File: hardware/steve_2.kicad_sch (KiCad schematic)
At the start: 24 parts, among them J6 MicroSD_Hirose_DM3AT, U2 TI_TPS51386RJNR_Regulator_Buc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, U6 W25Q128JVSIQ

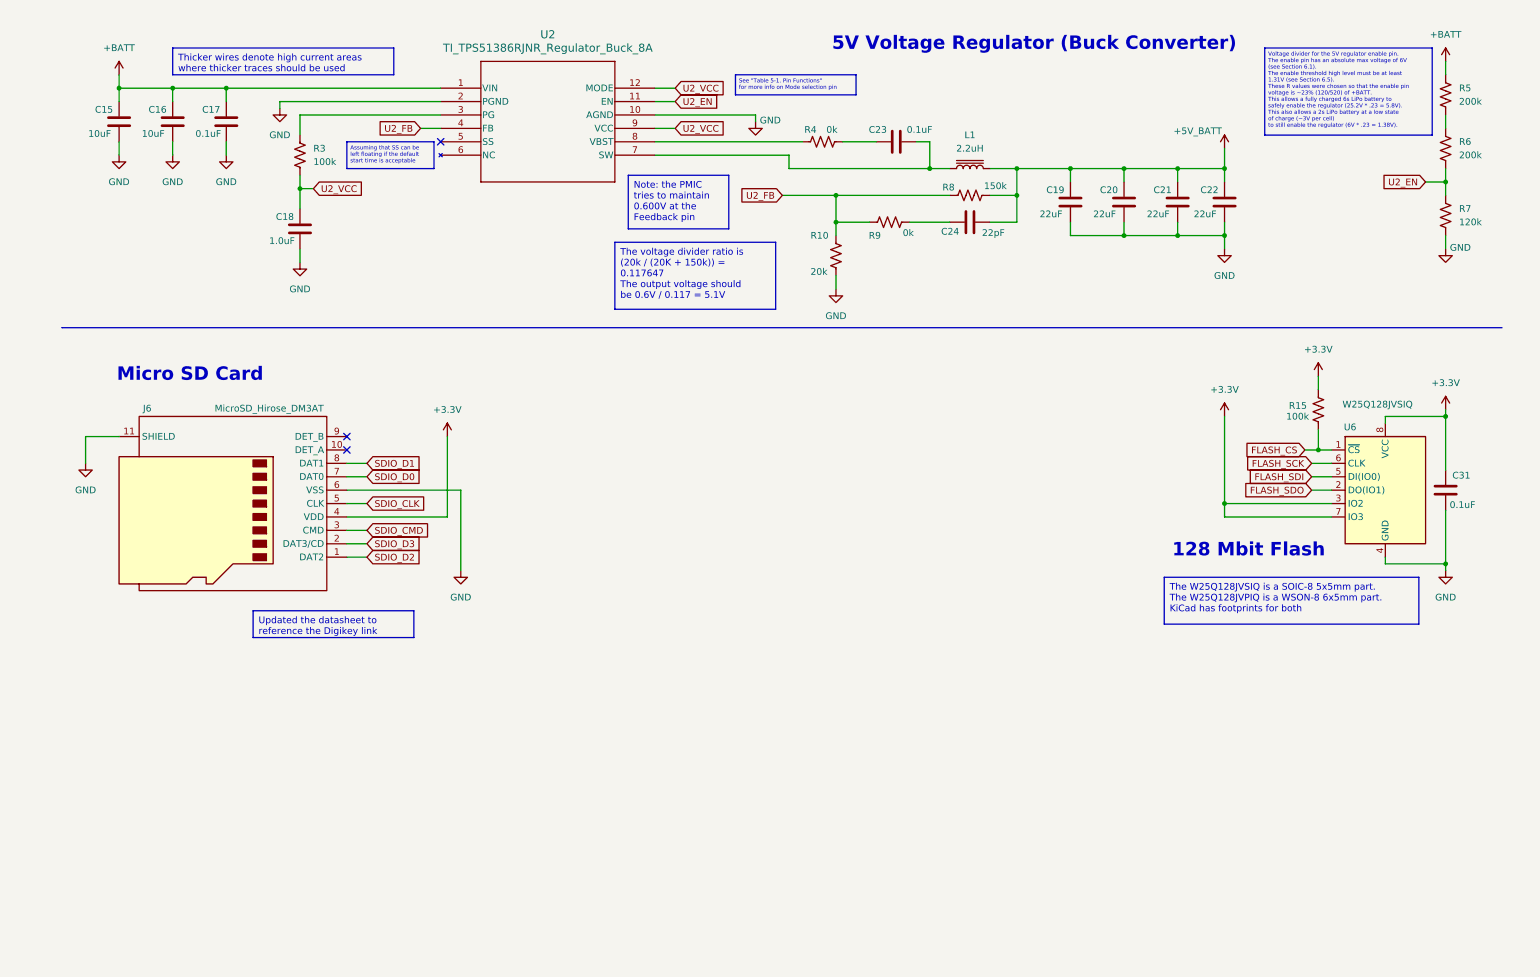
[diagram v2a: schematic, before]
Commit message: Add components to schematic; fix existing ones
Added additional components to schematic such as IO connectors. Replaced the 10A TO-263-2 diode rectifiers with much smaller 5A ones.
Other various fixes.
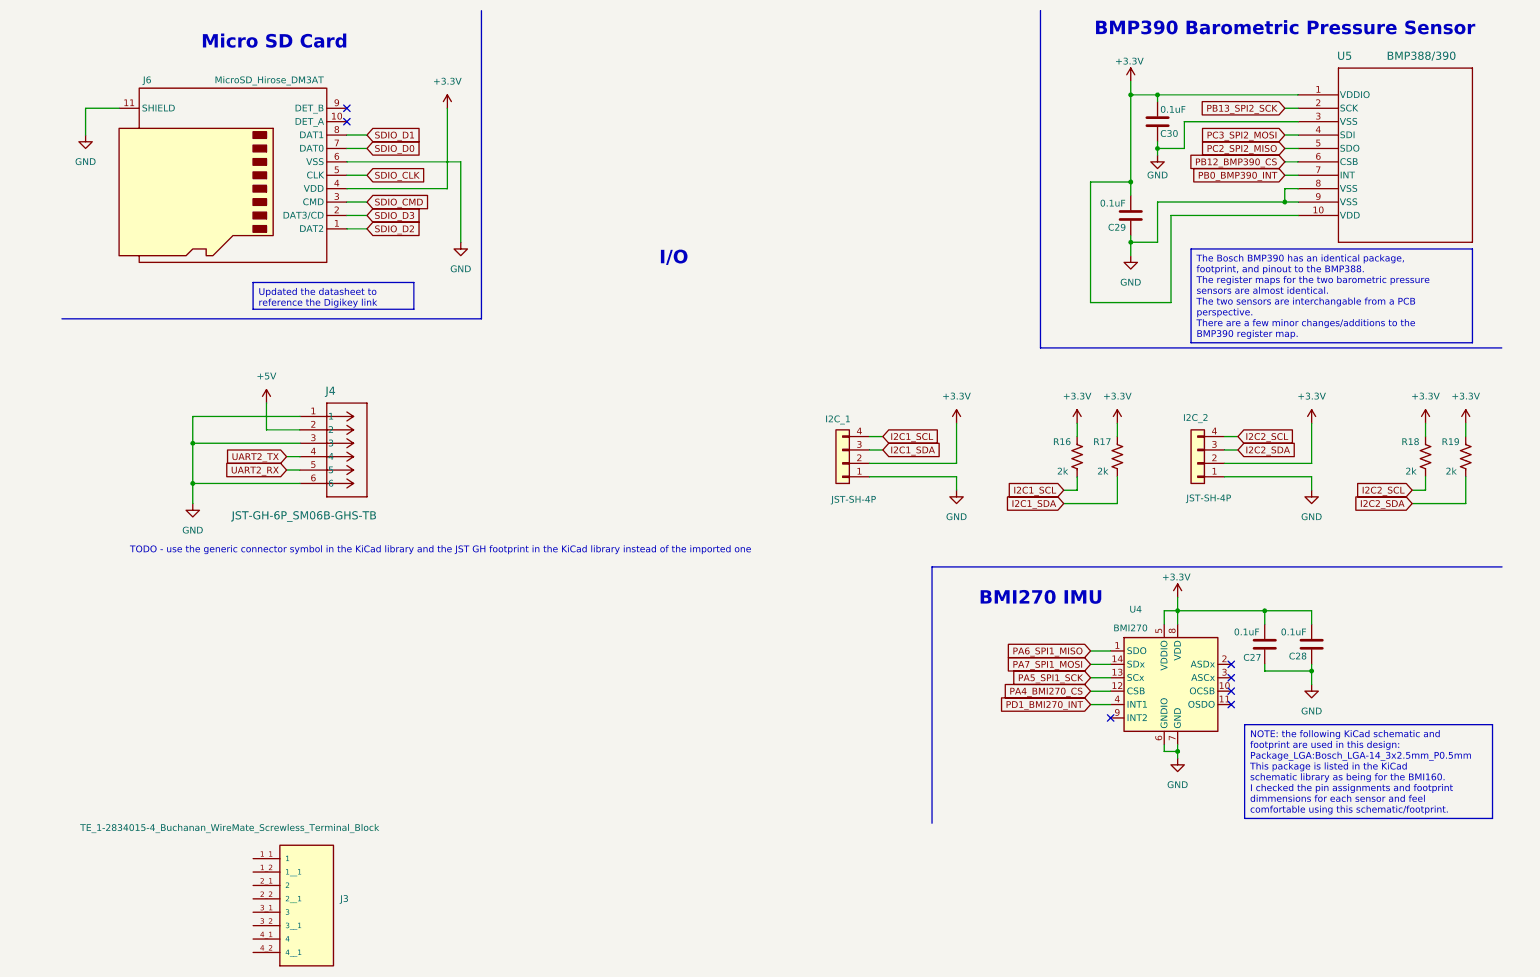
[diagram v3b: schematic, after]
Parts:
- removed C15, C16: 10uF, Capacitor_SMD:C_1206_3216Metric, symbol Device:C
- removed C17, C23, C31: 0.1uF, Capacitor_SMD:C_0603_1608Metric, symbol Device:C
- removed C18: 1.0uF, Capacitor_SMD:C_0603_1608Metric, symbol Device:C
- removed C19, C20, C21, C22: 22uF, Capacitor_SMD:C_1206_3216Metric, symbol Device:C
- removed C24: 22pF, Capacitor_SMD:C_0603_1608Metric, symbol Device:C
- removed L1: 2.2uH, Inductor_SMD:L_Coilcraft_XAL6060-XXX, symbol Device:L_Iron
- removed R10: 20k, Resistor_SMD:R_0603_1608Metric, symbol Device:R_US
- removed R15, R3: 100k, Resistor_SMD:R_0603_1608Metric, symbol Device:R_US
- removed R4, R9: 0k, Resistor_SMD:R_0603_1608Metric, symbol Device:R_US
- removed R5, R6: 200k, Resistor_SMD:R_0603_1608Metric, symbol Device:R_US
- removed R7: 120k, Resistor_SMD:R_0603_1608Metric, symbol Device:R_US
- removed R8: 150k, Resistor_SMD:R_0603_1608Metric, symbol Device:R_US
- removed U2: TI_TPS51386RJNR_Regulator_Buck_8A, Imported_Footprints:TI_TPS51386RJNR_VQFN-HR_REG_BUCK_8A, symbol Imported_Symbols:TI_TPS51386RJNR_Regulator_Buck_8A
- removed U6: W25Q128JVSIQ, Package_SO:SOIC-8_5.23x5.23mm_P1.27mm, symbol Memory_Flash:W25Q128JVS
- added C27, C28, C29, C30: 0.1uF, Capacitor_SMD:C_0603_1608Metric, symbol Device:C
- added I2C_1, I2C_2: JST-SH-4P, Imported_Footprints:JST-SH_BM04B-SRSS-TB_1x04_Vertical_P1.00mm, symbol Connector_Generic:Conn_01x04
- added J3: TE_1-2834015-4_Buchanan_WireMate_Screwless_Termin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, Imported_Footprints:TE_1-2834015-4_Buchanan_WireMate_Screwless_Terminal_Block, symbol Imported_Symbols:TE_1-2834015-4_Buchanan_WireMate_Screwless_Terminal_Block
- added J4: JST-GH-6P_SM06B-GHS-TB, Imported_Footprints:CONN_JST-GH-6P_SM06B-GHS-TB, symbol Imported_Symbols:JST-GH-6P_SM06B-GHS-TB
- added R16, R17, R18, R19: 2k, Resistor_SMD:R_0603_1608Metric, symbol Device:R_US
- added U4: BMI270, Package_LGA:Bosch_LGA-14_3x2.5mm_P0.5mm, symbol Sensor_Motion:BMI160
- added U5: BMP388/390, Imported_Footprints:QFN_BMP388_BOS, symbol Imported_Symbols:BMP388
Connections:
- net +3.3V: now also C27.1, C28.1, C29.1, C30.1, I2C_1.2 (Pin_2), I2C_2.2 (Pin_2), R16.2, R17.2, R18.2, R19.2, U4.5 (VDDIO), U4.8 (VDD), U5.1 (VDDIO), U5.10 (VDD)
- net GND: now also C27.2, C28.2, C29.2, C30.2, I2C_1.1 (Pin_1), I2C_2.1 (Pin_1), J4.1, J4.3, J4.6, U4.6 (GNDIO), U4.7 (GND), U5.3 (VSS), U5.8 (VSS), U5.9 (VSS)
- new net +5V: J4.2
- new net I2C1_SCL: I2C_1.4 (Pin_4), R16.1
- new net I2C1_SDA: I2C_1.3 (Pin_3), R17.1
- new net I2C2_SCL: I2C_2.4 (Pin_4), R18.1
- new net I2C2_SDA: I2C_2.3 (Pin_3), R19.1
- new net PA4_BMI270_CS: U4.12 (CSB)
- new net PA5_SPI1_SCK: U4.13 (SCx)
- new net PA6_SPI1_MISO: U4.1 (SDO)
- new net PA7_SPI1_MOSI: U4.14 (SDx)
- new net PB0_BMP390_INT: U5.7 (INT)
- new net PB12_BMP390_CS: U5.6 (CSB)
- new net PB13_SPI2_SCK: U5.2 (SCK)
- new net PC2_SPI2_MISO: U5.5 (SDO)
- new net PC3_SPI2_MOSI: U5.4 (SDI)
- new net PD1_BMI270_INT: U4.4 (INT1)
- new net UART2_RX: J4.5
- new net UART2_TX: J4.4
- no-connect marks 3 -> 7
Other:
- note added: "BMI270 IMU"
- note added: "BMP390 Barometric Pressure Sensor"
- note added: "I/O"
- note added: "TODO - use the generic connector symbol in the KiCad library and the JST GH footprint in the KiCad library instead of the imported one"
- note removed: "128 Mbit Flash"
- note removed: "5V Voltage Regulator (Buck Converter)"
- moved on the sheet: J6

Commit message: Added buzzer and LEDs to schematic
Added buzzer and LEDs (4 regular and 2 WS2812B) to schematic. Minor schematic fixes such as PMIC enable pin voltage divider.
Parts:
- added C32, C33: 0.1uF, Capacitor_SMD:C_0603_1608Metric, symbol Device:C
- added D3: RED, LED_SMD:LED_0603_1608Metric, symbol Device:LED
- added D4: Yellow, LED_SMD:LED_0603_1608Metric, symbol Device:LED
- added D5: GREEN, LED_SMD:LED_0603_1608Metric, symbol Device:LED
- added D6: BLUE, LED_SMD:LED_0603_1608Metric, symbol Device:LED
- added D7, D8: WS2812B, LED_SMD:LED_WS2812B_PLCC4_5.0x5.0mm_P3.2mm, symbol LED:WS2812B
- added LS1: Speaker, Buzzer_Beeper:Buzzer_Murata_PKMCS0909E, symbol Device:Speaker
- added Q1: Q_NMOS_GSD, Package_TO_SOT_SMD:SOT-23, symbol Device:Q_NMOS_GSD
- added R20, R21, R22, R26: 1k, Resistor_SMD:R_0603_1608Metric, symbol Device:R_US
- added R23, R24, R25: 220, Resistor_SMD:R_0603_1608Metric, symbol Device:R_US
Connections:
- net +5V: now also C32.1, C33.1, D7.1 (VDD), D8.1 (VDD), R21.2
- net GND: now also C32.2, C33.2, D3.1 (K), D4.1 (K), D5.1 (K), D6.1 (K), D7.3 (VSS), D8.3 (VSS), Q1.2 (S)
- new net: D4.2 (A), R24.2
- new net: Q1.1 (G), R22.2
- new net: LS1.2, Q1.3 (D), R20.1
- new net: D3.2 (A), R23.2
- new net: LS1.1, R20.2, R21.1
- new net: D7.2 (DOUT), D8.4 (DIN)
- new net: D6.2 (A), R26.2
- new net: D5.2 (A), R25.2
- new net Buzzer: R22.1
- new net LED1: R23.1
- new net LED2: R24.1
- new net LED3: R25.1
- new net LED4: R26.1
- new net LED_WS2812: D7.4 (DIN)
- no-connect marks 7 -> 8
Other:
- note added: "Buzzer"
- note added: "I2C"
- note added: "LED Resistor Calculator"
- note added: "LEDs"
- moved on the sheet: C27, C28, I2C_1, I2C_2, J3, J4, R16, R17, R18, R19, U4

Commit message: Removed PSM board components; added power conn; fixed telem conn
Moved PSM board components to the PSM board schematic.
Added a connector for the regulated 5V input to STEVE that comes from the PSM board.
Changed the radio telemetry connector to a 4 pin screwless terminal block to mitigate current limit concerns with the previous connector.
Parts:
- removed J4: JST-GH-6P_SM06B-GHS-TB, Imported_Footprints:CONN_JST-GH-6P_SM06B-GHS-TB, symbol Imported_Symbols:JST-GH-6P_SM06B-GHS-TB
- added J4: TerminalBlock_1770979_4pos_Vertical, Imported_Footprints:CONN_1814582_TerminalBlock_1770979_4pos_Vertical, symbol Imported_Symbols:TerminalBlock_1770979_4pos_Vertical
- added J7: TerminalBlock_1770885_2pos, Imported_Footprints:CONN_1814498_TerminalBlock-1770885-2pos, symbol Imported_Symbols:TerminalBlock_1770885_2pos
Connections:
- net +5V: now also J4.3, J4.4
- net GND: now also J4.1, J4.2, J7.3, J7.4
- net UART2_RX: now also J4.7, J4.8
- net UART2_TX: now also J4.5, J4.6
- new net +5V_BATT: J7.1, J7.2
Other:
- note added: "5V External Power"
- note added: "Telemetry Radio"

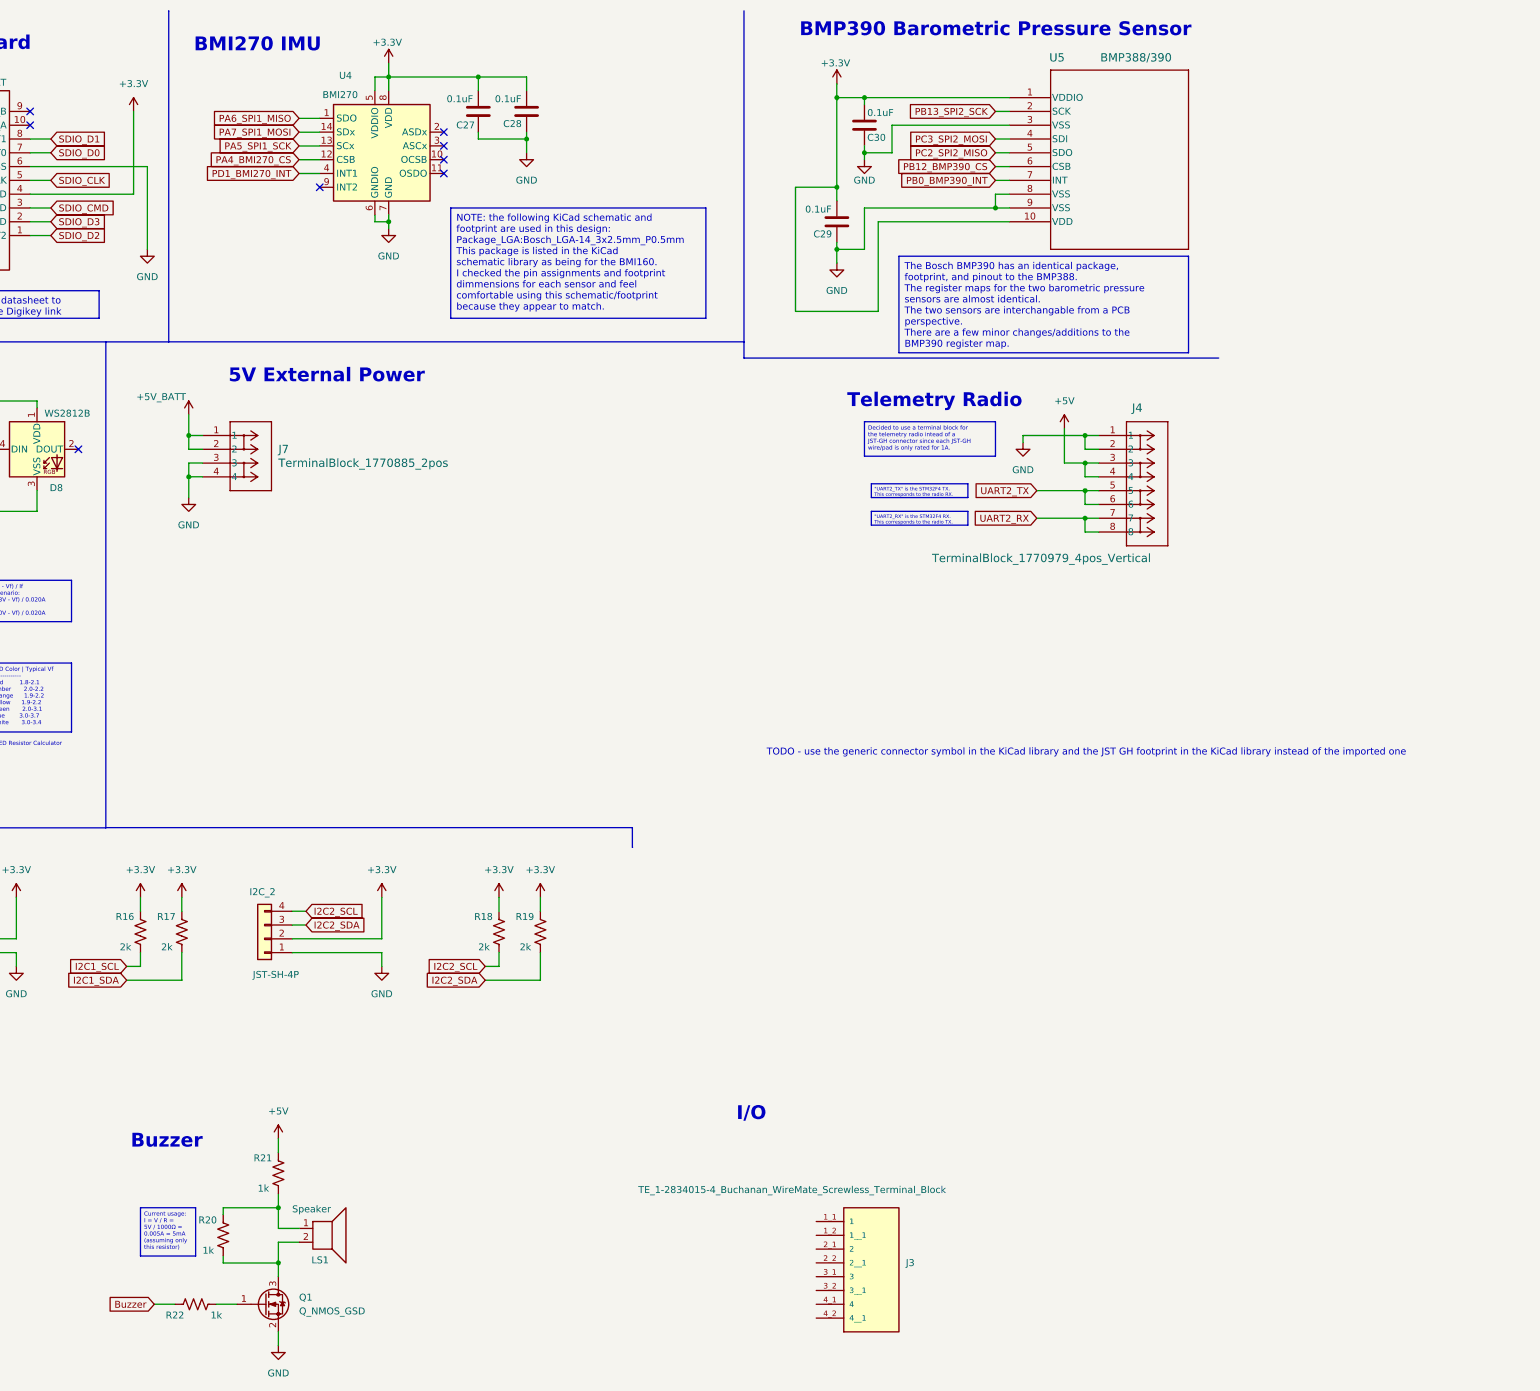
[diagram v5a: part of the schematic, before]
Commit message: Finished schematic
Finished schematic - 3D model fixes using custom imports, all important parts sourced, additional GPIO/bus pins broken out, PSM board signals broken out, battery voltage sense line added.
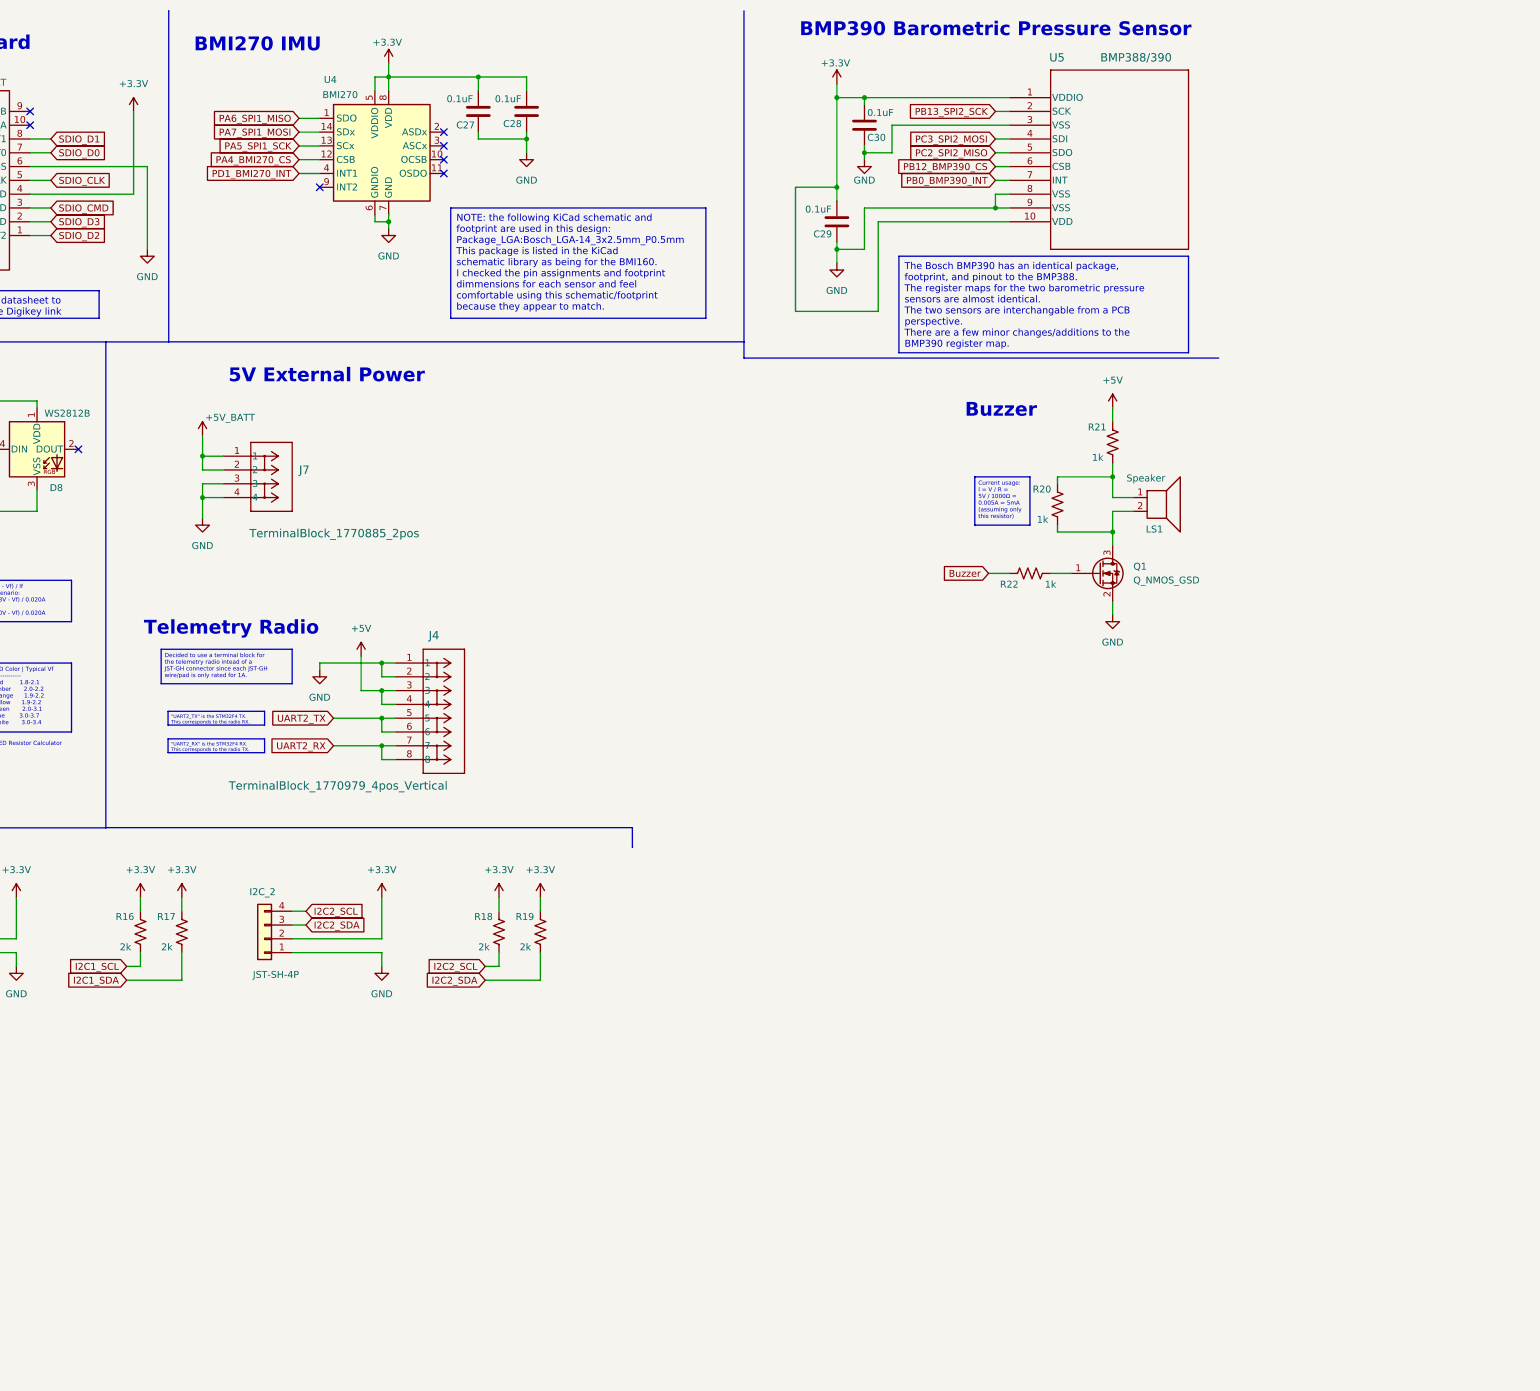
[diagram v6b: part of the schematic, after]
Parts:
- removed J3: TE_1-2834015-4_Buchanan_WireMate_Screwless_Termin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, Imported_Footprints:TE_1-2834015-4_Buchanan_WireMate_Screwless_Terminal_Block, symbol Imported_Symbols:TE_1-2834015-4_Buchanan_WireMate_Screwless_Terminal_Block
- J6: footprint Connector_Card:microSD_HC_Hirose_DM3AT-SF-PEJM5 -> Imported_Footprints:microSD_3D_HC_Hirose_DM3AT-SF-PEJM5
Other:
- note removed: "I/O"
- note removed: "TODO - use the generic connector symbol in the KiCad library and the JST GH footprint in the KiCad library instead of the imported one"
- moved on the sheet: J4, J7, LS1, Q1, R20, R21, R22
